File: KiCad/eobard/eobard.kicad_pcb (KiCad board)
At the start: 2 copper layers, 125 x 109 mm, 64 parts, among them J1 UART JACK LEFT, J2 RIGHT SSD1306 0.91 OLED 4pin, J3 UART Jack Right, J4 LEFT SSD1306 0.91 OLED 4pin, SW1 SW_SPST, SW10 SW_SPST, SW11 SW_SPST, SW12 SW_SPST, SW13 SW_SPST, SW14 SW_SPST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

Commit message: Updated KiCad Files
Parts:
- removed G: LOGO, Eobard-SVG-Files:ADHD-Creature_large
- removed the G*** at (82.0, 98.2) (x2)
- removed the G*** at (119.0, 64.4) (x2)
- removed the G*** at (159.7, 103.4) (x2)
- removed the G*** at (175.4, 47.1)
- moved G*** 20.4 mm to (143.9, 109.7) (x2)
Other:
- outline, holes or cut-outs redrawn
- board text added: "REV 2.3"
- board text removed: "REV 2.2"

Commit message: Updated KiCad Files
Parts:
- moved G*** 3.15 mm to (147.0, 110.0) (x2)
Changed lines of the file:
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@@
   (title_block
     (title "Eobard Split Keyboard")
-    (date "2023-12-10")
-    (rev "2.2")
+    (date "2024-01-08")
+    (rev "2.3")
     (company "by viniciusbrit")
   )
@@
   )
   (footprint "Eobard-SVG-Files:ADHD-Creature" (layer "F.Cu")
-    (at 143.8656 109.728)
+    (at 147 110)
     (attr board_only exclude_from_pos_files exclude_from_bom)
     (fp_text reference "G***" (at 0 -8.128) (layer "F.SilkS") hide
@@
   )
   (footprint "Eobard-SVG-Files:ADHD-Creature" (layer "B.Cu")
-    (at 143.8656 109.728 180)
+    (at 147 110 180)
     (attr board_only exclude_from_pos_files exclude_from_bom)
     (fp_text reference "G***" (at 0 8.128) (layer "B.SilkS") hide

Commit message: Fixed Silkscreen Error & Changed Mounting Hole Position
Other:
- outline, holes or cut-outs redrawn
- board text added: "REV 2.4"
- board text removed: "REV 2.3"
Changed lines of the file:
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@@
   (title_block
     (title "Eobard Split Keyboard")
-    (date "2024-01-08")
-    (rev "2.3")
+    (date "2024-01-12")
+    (rev "2.4")
     (company "by viniciusbrit")
   )
@@
   (gr_circle (center 176.5 106.5) (end 176.5 107.5)
     (stroke (width 0.1) (type default)) (fill none) (layer "Edge.Cuts"))
-  (gr_circle (center 123.952 109.6772) (end 123.952 110.6772)
+  (gr_circle (center 127 109.6772) (end 127 110.6772)
     (stroke (width 0.1) (type default)) (fill none) (layer "Edge.Cuts"))
   (gr_rect (start 191.25 62.5) (end 195.5 67.5)
@@
   (gr_circle (center 194 130) (end 194 131)
     (stroke (width 0.1) (type default)) (fill none) (layer "Edge.Cuts"))
-  (gr_text "REV 2.3" (at 198 112.1 90) (layer "F.Cu")
+  (gr_text "REV 2.4" (at 198 112.1 90) (layer "F.Cu")
     (effects (font (size 1 1) (thickness 0.2) bold italic) (justify left bottom))
   )
-  (gr_text "REV 2.3" (at 196.7 112 270) (layer "B.Cu")
+  (gr_text "REV 2.4" (at 196.7 112 270) (layer "B.Cu")
     (effects (font (size 1 1) (thickness 0.2) bold italic) (justify left bottom mirror))
   )
-  (gr_text "LEFT" (at 184.5 111.5) (layer "B.SilkS")
+  (gr_text "RIGHT" (at 184.5 111.5) (layer "B.SilkS")
     (effects (font (size 1 1) (thickness 0.2) bold italic) (justify left bottom mirror))
   )
@@
     (effects (font (size 1 1) (thickness 0.2) bold italic) (justify bottom mirror))
   )
-  (gr_text "RIGHT" (at 180 107.75) (layer "F.SilkS")
+  (gr_text "LEFT" (at 180 107.75) (layer "F.SilkS")
     (effects (font (size 1 1) (thickness 0.2) bold italic) (justify left bottom))
   )

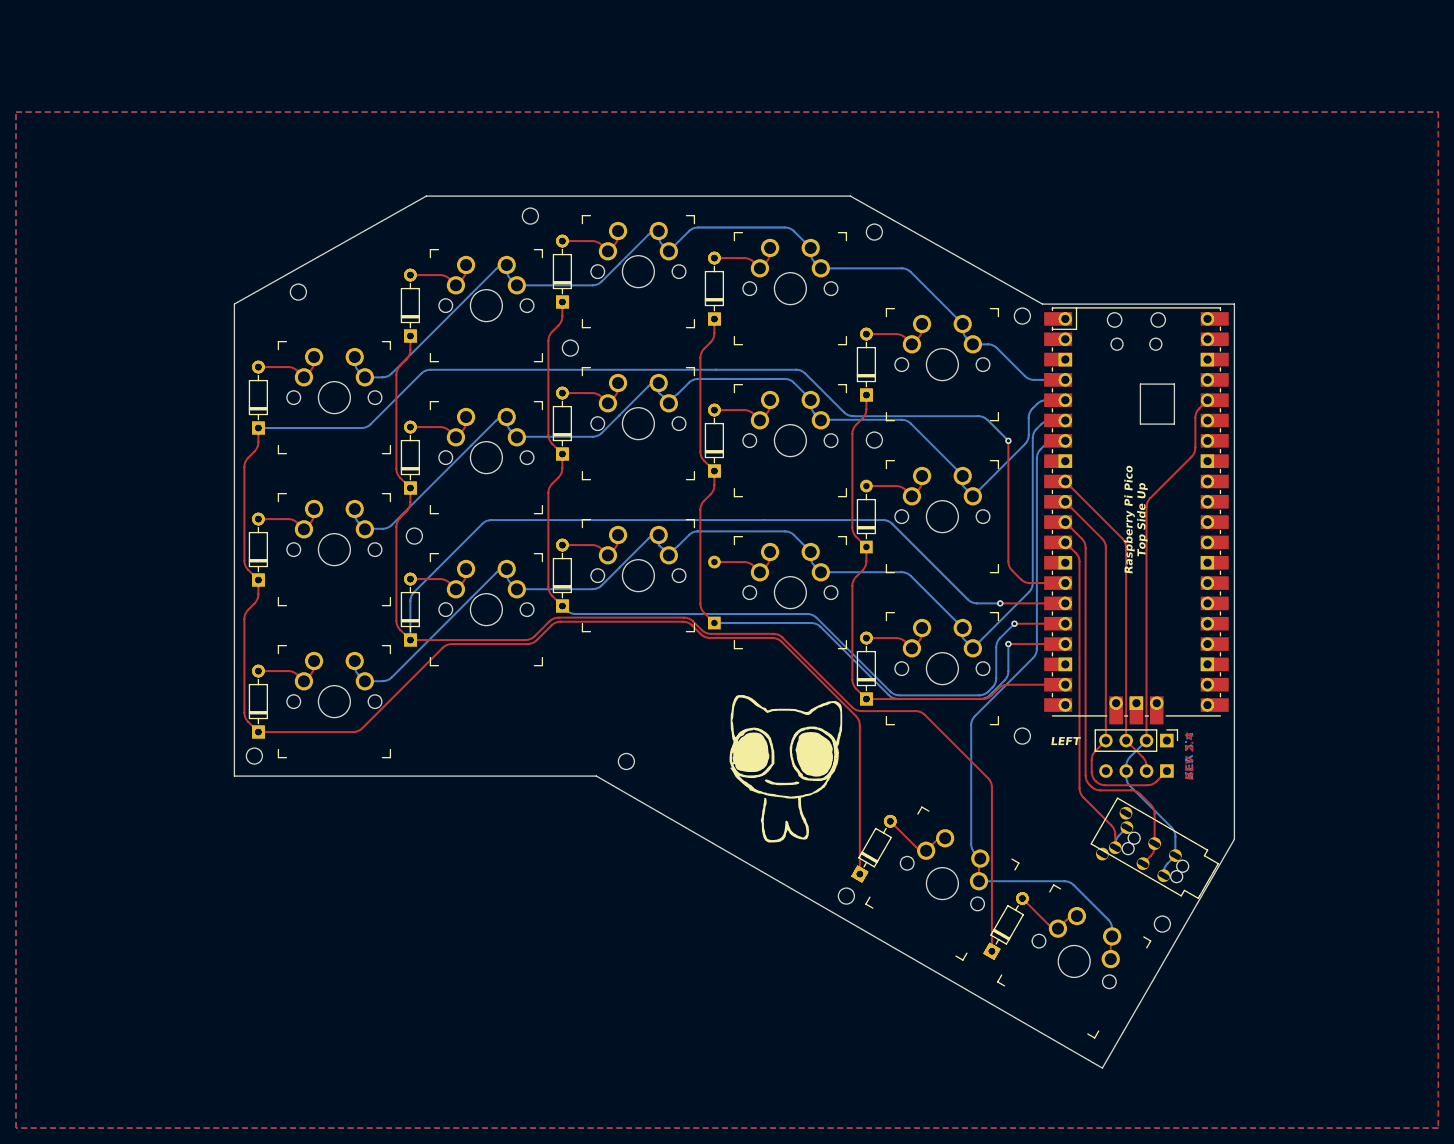
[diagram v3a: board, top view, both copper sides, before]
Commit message: Fixed Footprint Error
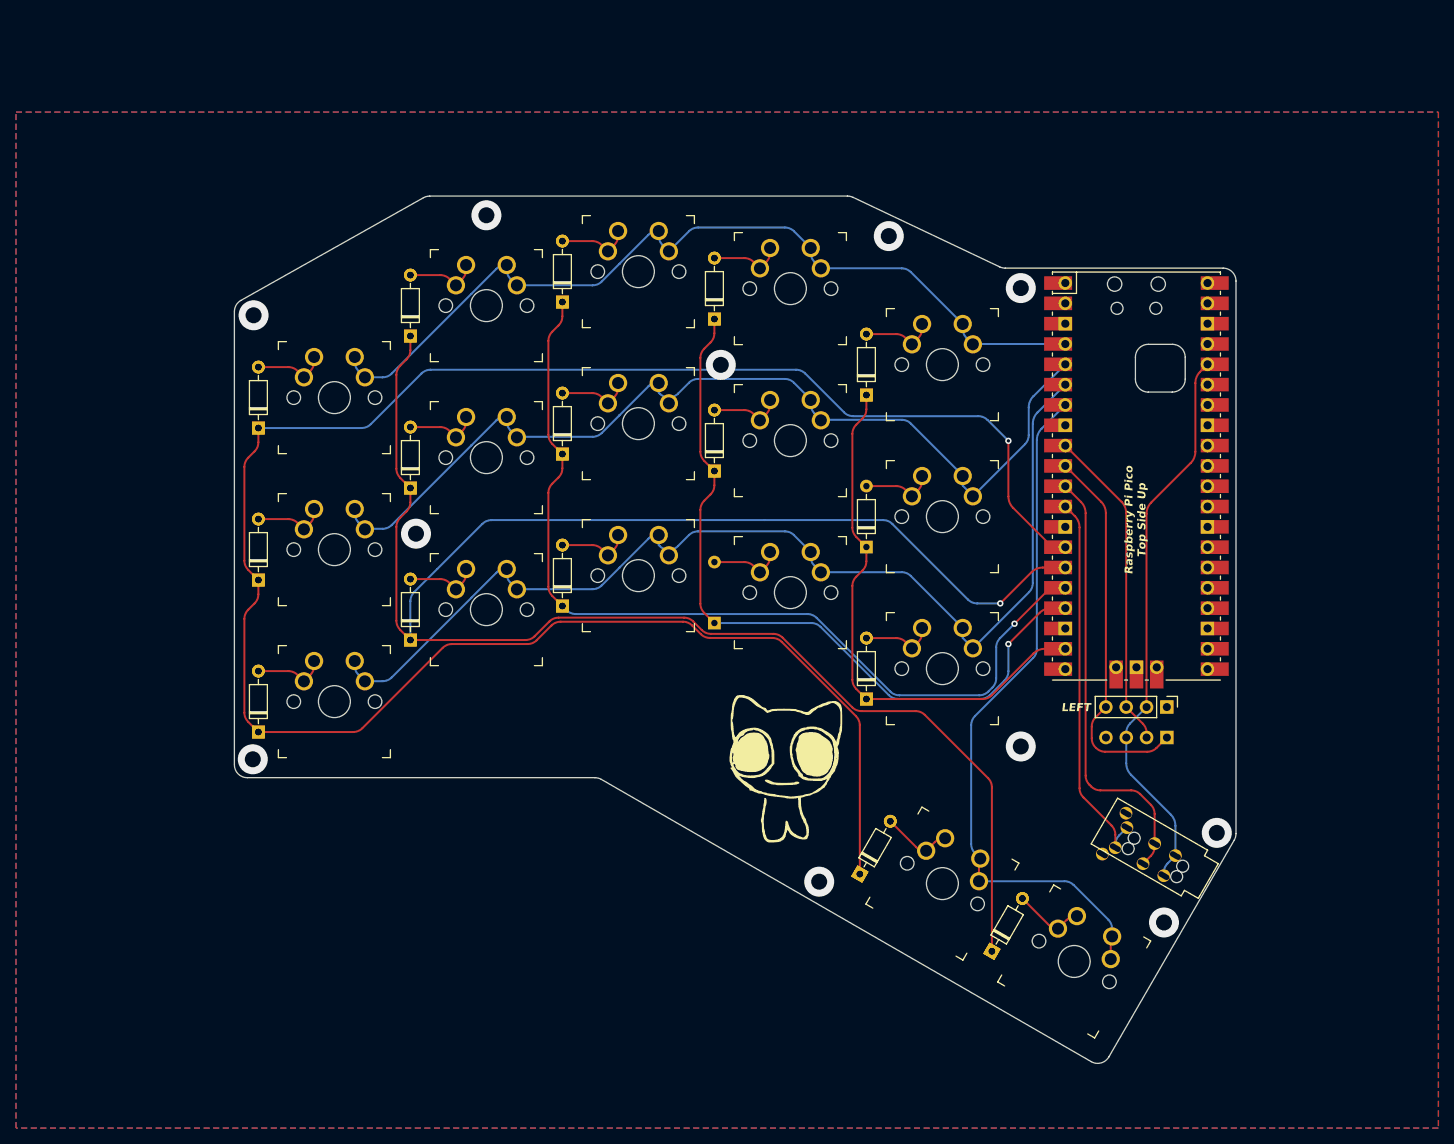
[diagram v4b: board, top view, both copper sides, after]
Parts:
- moved U1 4.49 mm to (190.8, 74.0)
- moved J4 4.19 mm to (194.6, 102.9)
- moved J2 4.19 mm to (194.6, 106.7)
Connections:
- D1 pad 1: (no net) -> COL1
- D1 pad 2: (no net) -> Net-(D1-A)
- D11 pad 1: (no net) -> COL1
- D11 pad 2: (no net) -> Net-(D11-A)
- D12 pad 1: (no net) -> COL2
- D12 pad 2: (no net) -> Net-(D12-A)
- D13 pad 1: (no net) -> COL3
- D13 pad 2: (no net) -> Net-(D13-A)
- D15 pad 1: (no net) -> COL5
- D15 pad 2: (no net) -> Net-(D15-A)
- D16 pad 1: (no net) -> COL1
- D16 pad 2: (no net) -> Net-(D16-A)
- D17 pad 1: (no net) -> COL2
- D17 pad 2: (no net) -> Net-(D17-A)
- D2 pad 1: (no net) -> COL2
- D2 pad 2: (no net) -> Net-(D2-A)
- D3 pad 1: (no net) -> COL3
- D3 pad 2: (no net) -> Net-(D3-A)
- D4 pad 1: (no net) -> COL4
- D4 pad 2: (no net) -> Net-(D4-A)
- D5 pad 1: (no net) -> COL5
- D5 pad 2: (no net) -> Net-(D5-A)
- D6 pad 1: (no net) -> COL1
- D6 pad 2: (no net) -> Net-(D6-A)
- D7 pad 1: (no net) -> COL2
- D7 pad 2: (no net) -> Net-(D7-A)
- D8 pad 1: (no net) -> COL3
- D8 pad 2: (no net) -> Net-(D8-A)
- D9 pad 1: (no net) -> COL4
- D9 pad 2: (no net) -> Net-(D9-A)
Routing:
- net COL1: track 268.7 -> 262.1 mm
- net UART TX: track 50.5 -> 55.0 mm
- net UART RX: track 43.5 -> 48.0 mm
- net VCC: track 66.2 -> 70.6 mm
- net LINE4: track 84.5 -> 87.8 mm
- net LINE3: track 132.7 -> 135.8 mm
- net LINE2: track 116.6 -> 119.3 mm
- net COL5: track 65.9 -> 67.7 mm
- net COL3: track 114.2 -> 116.0 mm
- net COL4: track 93.1 -> 94.9 mm
- net COL2: track 238.7 -> 240.4 mm
- net LINE1: track 112.4 -> 110.7 mm
- net (no net): vias 0 -> 11
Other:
- board size 125 x 109 mm -> 125.2 x 108.4 mm
- board text removed: "REV 2.4"
